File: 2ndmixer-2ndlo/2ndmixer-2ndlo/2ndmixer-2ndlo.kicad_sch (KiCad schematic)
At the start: 58 parts, among them J201 Coax Solder Point, J202 Conn_01x02, J203 Coax Solder Point, Q201 2N5179, Q202 2N5179, T201 Bifilar_Transformer, U201 MAV-11, U202 TUF-1H+, Y201 100MHz

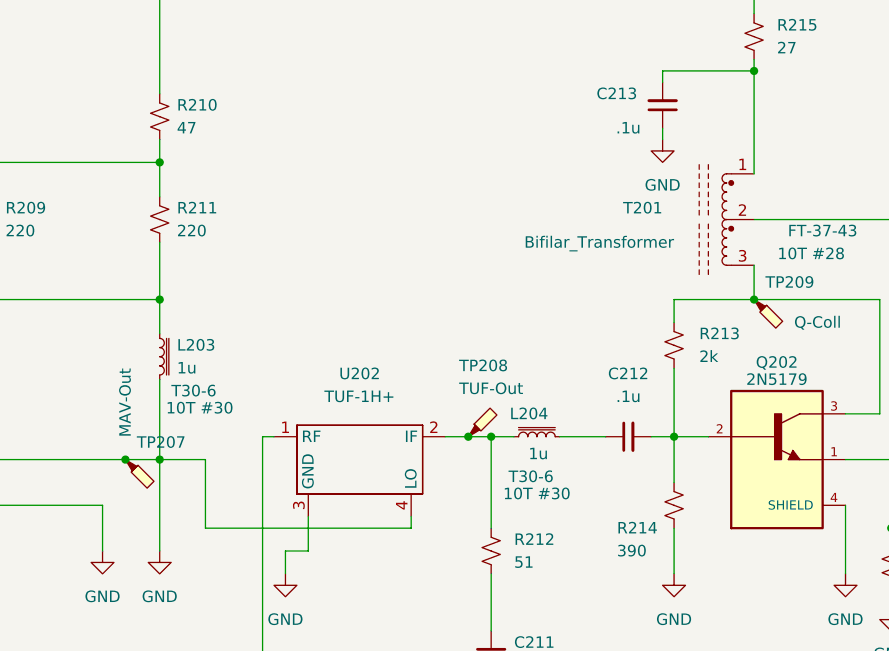
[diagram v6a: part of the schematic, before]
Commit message: Fixes to 2ndmixer-2ndlo and vco-1stmixer
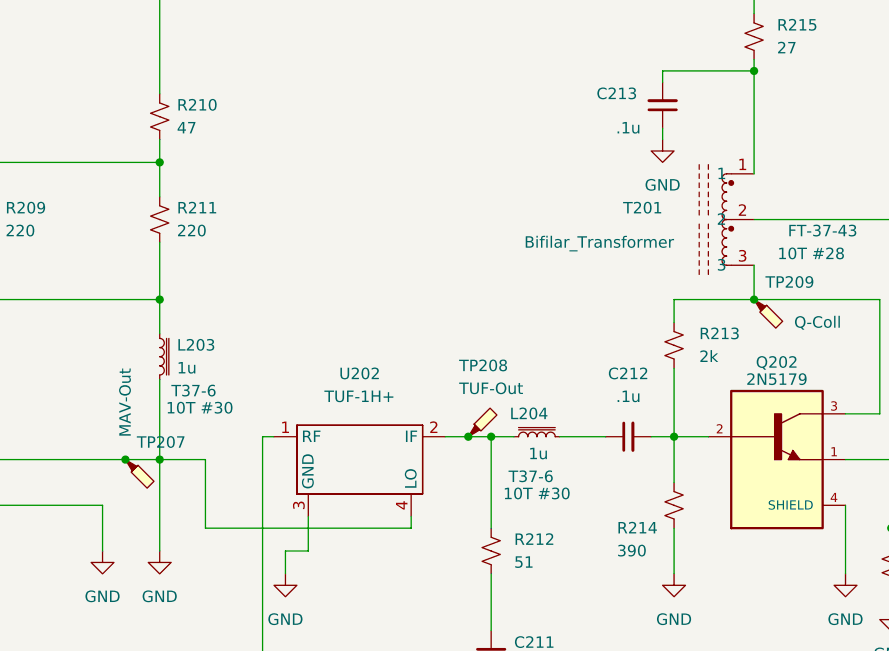
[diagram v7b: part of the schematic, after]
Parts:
- C202: footprint 2ndmixer-2ndlo:DSS1NB32A102Q91A -> spectrum_analyzer:DSS1NB32A102Q91A
- C206: footprint 2ndmixer-2ndlo:GKG60015 -> spectrum_analyzer:GKG60015
- J202: footprint 2ndmixer-2ndlo:691103110002 -> spectrum_analyzer:691103110002
- L203, L204: Field4 T30-6 -> T37-6
- Q201: footprint 2ndmixer-2ndlo:TO127P584H533-4N -> spectrum_analyzer:TO127P584H533-4N; symbol 2ndmixer-2ndlo:2N5179 -> spectrum_analyzer:2N5179
- Q202: footprint 2ndmixer-2ndlo:TO127P584H533-4N -> spectrum_analyzer:TO127P584H533-4N
- T201: symbol 2ndmixer-2ndlo:Bifilar_Transformer -> spectrum_analyzer:Bifilar_Transformer
- U201: footprint 2ndmixer-2ndlo:MAV-11BSM&plus_ -> spectrum_analyzer:MAV-11BSM&plus_; symbol 2ndmixer-2ndlo:MAV-11 -> spectrum_analyzer:MAV-11
- U202: symbol 2ndmixer-2ndlo:TUF-1H+ -> spectrum_analyzer:TUF-1H+
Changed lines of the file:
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@@
     (rev "0")
     (company "Andy McCann KA3KAF and Doug McCann KA3KAG")
-    (comment 2 "Wes Hayward W7ZOI")
-    (comment 3 "Original Design By:")
+    (comment 1 "https://www.kangaus.com/documentation/New%20SA/Second_LO_SCH.pdf")
+    (comment 2 "As modified by Kanga US schematic:")
+    (comment 3 "Wes Hayward W7ZOI")
+    (comment 4 "Original Design By:")
   )
   (junction (at 172.72 130.81) (diameter 0) (color 0 0 0 0)
@@
     (pin "1")
   )
-  (symbol (lib_id "2ndmixer-2ndlo:MAV-11") (at 184.15 120.65 0) (unit 1)
+  (symbol (lib_id "spectrum_analyzer:MAV-11") (at 184.15 120.65 0) (unit 1)
     (in_bom yes) (on_board yes) (fields_autoplaced)
     (property "Reference" "U201" (id 0) (at 196.85 116.0333 0))
     (property "Value" "MAV-11" (id 1) (at 196.85 118.5733 0))
-    (property "Footprint" "2ndmixer-2ndlo:MAV-11BSM&plus_" (id 2) (at 184.15 120.65 0)
+    (property "Footprint" "spectrum_analyzer:MAV-11BSM&plus_" (id 2) (at 184.15 120.65 0)
       (effects (font (size 1.27 1.27)) hide)
     )
@@
       (effects (font (size 1.27 1.27)) hide)
     )
-    (property "Field4" "T30-6" (id 4) (at 271.145 125.095 90))
+    (property "Field4" "T37-6" (id 4) (at 271.145 125.095 90))
     (property "Field5" "10T #30" (id 5) (at 271.78 127 90))
     (pin "1")
@@
     (pin "2")
   )
-  (symbol (lib_id "2ndmixer-2ndlo:TUF-1H+") (at 251.46 123.19 0) (unit 1)
+  (symbol (lib_id "spectrum_analyzer:TUF-1H+") (at 251.46 123.19 0) (unit 1)
     (in_bom yes) (on_board yes) (fields_autoplaced)
     (property "Reference" "U202" (id 0) (at 252.095 113.665 0))
@@
     (pin "2")
   )
-  (symbol (lib_id "2ndmixer-2ndlo:2N5179") (at 58.42 119.38 0) (unit 1)
+  (symbol (lib_id "spectrum_analyzer:2N5179") (at 58.42 119.38 0) (unit 1)
     (in_bom yes) (on_board yes) (fields_autoplaced)
     (property "Reference" "Q201" (id 0) (at 58.42 106.045 0))
     (property "Value" "2N5179" (id 1) (at 58.42 108.585 0))
-    (property "Footprint" "2ndmixer-2ndlo:TO127P584H533-4N" (id 2) (at 58.42 119.38 0)
+    (property "Footprint" "spectrum_analyzer:TO127P584H533-4N" (id 2) (at 58.42 119.38 0)
       (effects (font (size 1.27 1.27)) (justify left bottom) hide)
     )
@@
     (pin "2")
   )
-  (symbol (lib_id "2ndmixer-2ndlo:Bifilar_Transformer") (at 289.56 96.52 270) (unit 1)
+  (symbol (lib_id "spectrum_analyzer:Bifilar_Transformer") (at 289.56 96.52 270) (unit 1)
     (in_bom yes) (on_board yes)
     (property "Reference" "T201" (id 0) (at 285.75 95.25 90)
@@
       (effects (font (size 1.27 1.27)) (justify right))
     )
-    (property "Footprint" "Transformer_THT:Autotransformer_Toroid_1Tap_Horizontal_D10.5mm_Amidon-T37" (id 2) (at 289.56 96.52 0)
-      (effects (font (size 1.27 1.27)) hide)
-    )
-    (property "Datasheet" "" (id 3) (at 289.56 96.52 0)
+    (property "Footprint" "Transformer_THT:Autotransformer_Toroid_1Tap_Horizontal_D10.5mm_Amidon-T37" (id 2) (at 292.735 90.17 0)
+      (effects (font (size 1.27 1.27)) hide)
+    )
+    (property "Datasheet" "" (id 3) (at 292.735 90.17 0)
       (effects (font (size 1.27 1.27)) hide)
     )
@@
       (effects (font (size 1.27 1.27)) hide)
     )
-    (property "Field4" "T30-6" (id 4) (at 233.68 115.57 0))
+    (property "Field4" "T37-6" (id 4) (at 233.68 115.57 0))
     (property "Field5" "10T #30" (id 5) (at 234.315 117.475 0))
     (pin "1")
@@
       (effects (font (size 1.27 1.27)) (justify right))
     )
-    (property "Footprint" "2ndmixer-2ndlo:691103110002" (id 2) (at 49.53 80.01 0)
+    (property "Footprint" "spectrum_analyzer:691103110002" (id 2) (at 49.53 80.01 0)
       (effects (font (size 1.27 1.27)) hide)
     )
@@
     (property "Reference" "C202" (id 0) (at 31.75 63.5 0))
     (property "Value" "1n" (id 1) (at 31.75 66.04 0))
-    (property "Footprint" "2ndmixer-2ndlo:DSS1NB32A102Q91A" (id 2) (at 31.75 72.39 90)
+    (property "Footprint" "spectrum_analyzer:DSS1NB32A102Q91A" (id 2) (at 31.75 72.39 90)
       (effects (font (size 1.27 1.27)) hide)
     )
@@
       (effects (font (size 1.27 1.27)) (justify left))
     )
-    (property "Footprint" "2ndmixer-2ndlo:GKG60015" (id 2) (at 104.14 118.11 0)
+    (property "Footprint" "spectrum_analyzer:GKG60015" (id 2) (at 104.14 118.11 0)
       (effects (font (size 1.27 1.27)) hide)
     )
@@
     (property "Reference" "Q202" (id 0) (at 298.45 112.395 0))
     (property "Value" "2N5179" (id 1) (at 298.45 114.3 0))
-    (property "Footprint" "2ndmixer-2ndlo:TO127P584H533-4N" (id 2) (at 298.45 123.19 0)
+    (property "Footprint" "spectrum_analyzer:TO127P584H533-4N" (id 2) (at 298.45 123.19 0)
       (effects (font (size 1.27 1.27)) (justify left bottom) hide)
     )
@@
     )
     (path "/d652cd25-7d8e-46b1-8b61-c2a4cab909b0"
-      (reference "C202") (unit 1) (value "1n") (footprint "2ndmixer-2ndlo:DSS1NB32A102Q91A")
+      (reference "C202") (unit 1) (value "1n") (footprint "spectrum_analyzer:DSS1NB32A102Q91A")
     )
     (path "/dec4d80a-8839-4da5-a1cc-dd685ff54b99"
@@
     )
     (path "/d8ed3cd9-959d-4947-a7a0-77b8ad7d1cc3"
-      (reference "C206") (unit 1) (value "12p-60p") (footprint "2ndmixer-2ndlo:GKG60015")
+      (reference "C206") (unit 1) (value "12p-60p") (footprint "spectrum_analyzer:GKG60015")
     )
     (path "/2e5d45e1-bdd9-4d08-bfbd-513f242495db"
@@
     )
     (path "/a6611718-7fc2-414e-a236-257a06874737"
-      (reference "J202") (unit 1) (value "Conn_01x02") (footprint "2ndmixer-2ndlo:691103110002")
+      (reference "J202") (unit 1) (value "Conn_01x02") (footprint "spectrum_analyzer:691103110002")
     )
     (path "/93f4dd11-35f6-40b0-9297-90dcba41f11b"
@@
     )
     (path "/4e6ebc34-5bf1-4c88-90bc-19a8769e1e49"
-      (reference "Q201") (unit 1) (value "2N5179") (footprint "2ndmixer-2ndlo:TO127P584H533-4N")
+      (reference "Q201") (unit 1) (value "2N5179") (footprint "spectrum_analyzer:TO127P584H533-4N")
     )
     (path "/ea7a5f2d-4da0-4cf0-a51f-1fa9370b1e84"
-      (reference "Q202") (unit 1) (value "2N5179") (footprint "2ndmixer-2ndlo:TO127P584H533-4N")
+      (reference "Q202") (unit 1) (value "2N5179") (footprint "spectrum_analyzer:TO127P584H533-4N")
     )
     (path "/b861b937-5868-48ec-8981-22e5f8da6e96"
@@
     )
     (path "/2b269c59-d9c7-4321-a64d-f838ca5a5591"
-      (reference "U201") (unit 1) (value "MAV-11") (footprint "2ndmixer-2ndlo:MAV-11BSM&plus_")
+      (reference "U201") (unit 1) (value "MAV-11") (footprint "spectrum_analyzer:MAV-11BSM&plus_")
     )
     (path "/4b92b6cd-ecaa-4fa9-91f6-6c221e287382"

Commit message: v7 conversion
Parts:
- J201, J203: Spice_Model Conn_Coaxial -> (none); Spice_Netlist_Enabled N -> (none); Spice_Primitive J -> (none)
- J202: Spice_Model Conn_01x02 -> (none); Spice_Netlist_Enabled N -> (none); Spice_Primitive J -> (none)
- Q201, Q202: Spice_Lib_File 2ndmixer-2ndlo-spice\2N5179.LIB -> (none); Spice_Model 2N5179 -> (none); Spice_Netlist_Enabled Y -> (none); Spice_Primitive Q -> (none)
- TP201: value Q-Base -> ${SIM.PARAMS}; Spice_Netlist_Enabled N -> (none)
- TP202: value +15 -> ${SIM.PARAMS}; Spice_Netlist_Enabled N -> (none)
- TP203, TP209: value Q-Coll -> ${SIM.PARAMS}; Spice_Netlist_Enabled N -> (none)
- TP204: value 6db Pad In -> ${SIM.PARAMS}; Spice_Netlist_Enabled N -> (none)
- TP205: value 6db Pad Out -> ${SIM.PARAMS}; Spice_Netlist_Enabled N -> (none)
- TP206: value MAV-In -> ${SIM.PARAMS}; Spice_Netlist_Enabled N -> (none)
- TP207: value MAV-Out -> ${SIM.PARAMS}; Spice_Netlist_Enabled N -> (none)
- TP208: value TUF-Out -> ${SIM.PARAMS}; Spice_Netlist_Enabled N -> (none)
- TP210: value Q-Emit -> ${SIM.PARAMS}; Spice_Netlist_Enabled N -> (none)
